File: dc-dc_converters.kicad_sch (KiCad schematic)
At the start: 63 parts, among them J3 JST_SH_1x4_SM04B-SRSS-TB-LF-SN, J4 Molex_Nano-Fit_1x2_105313-220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, U2 SIC477ED-T1-GE3, U3 AP62301Z6-7, U4 AP62301Z6-7

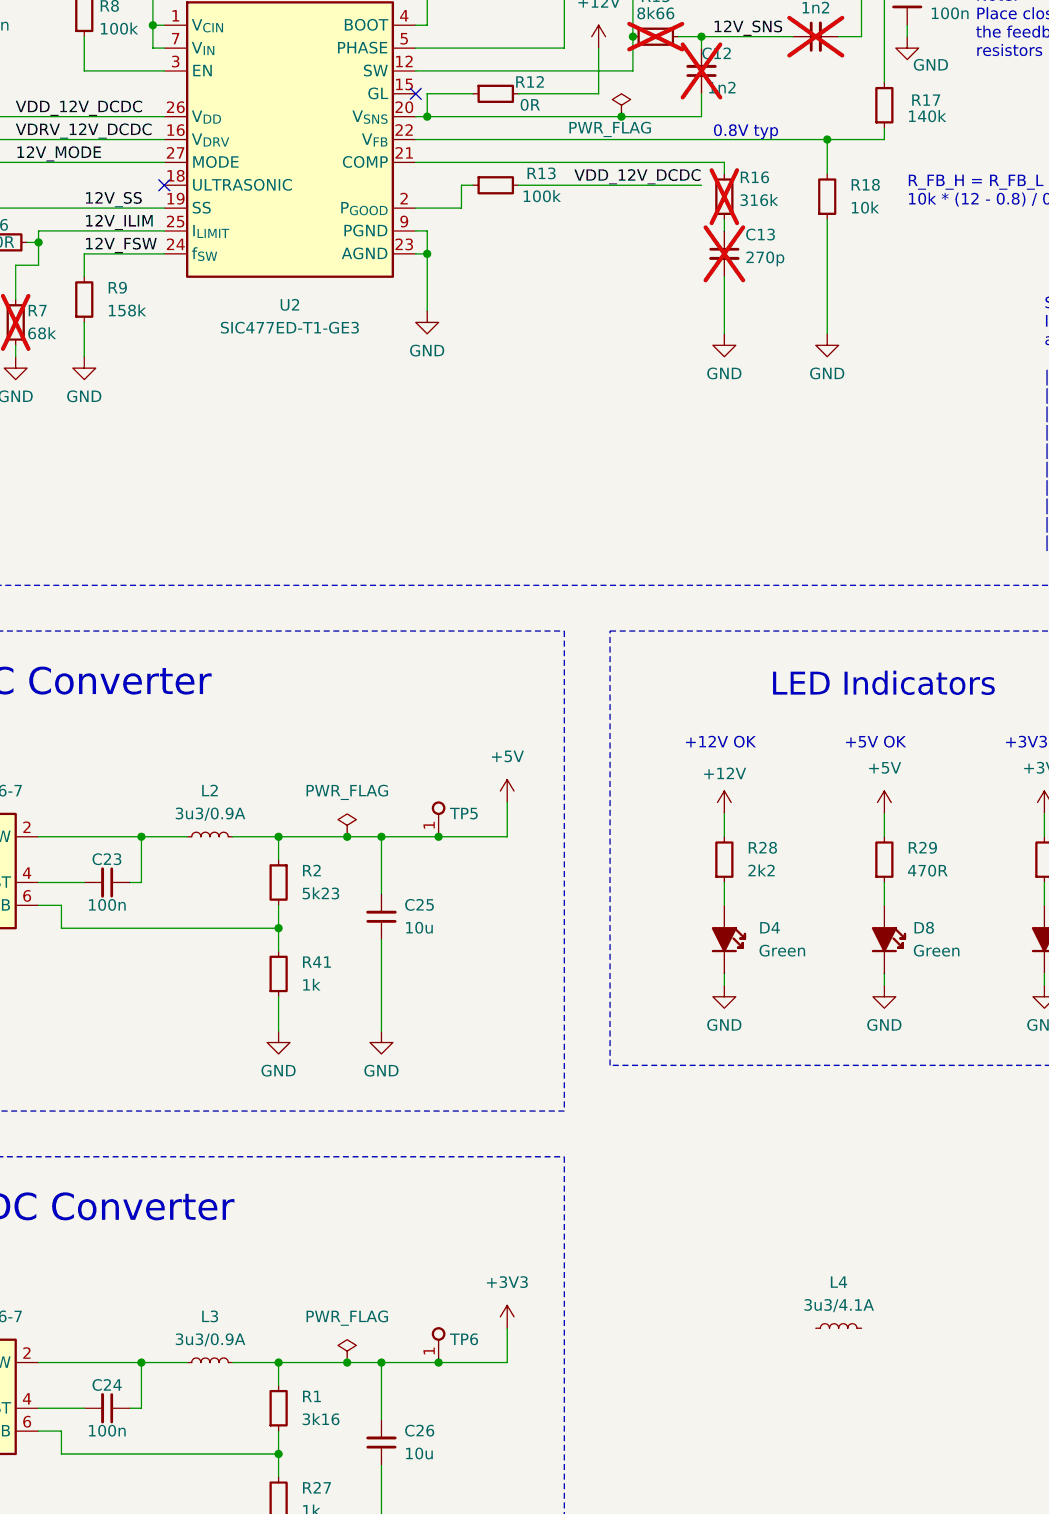
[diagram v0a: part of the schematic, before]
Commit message: [#57006] Change L2 and L3
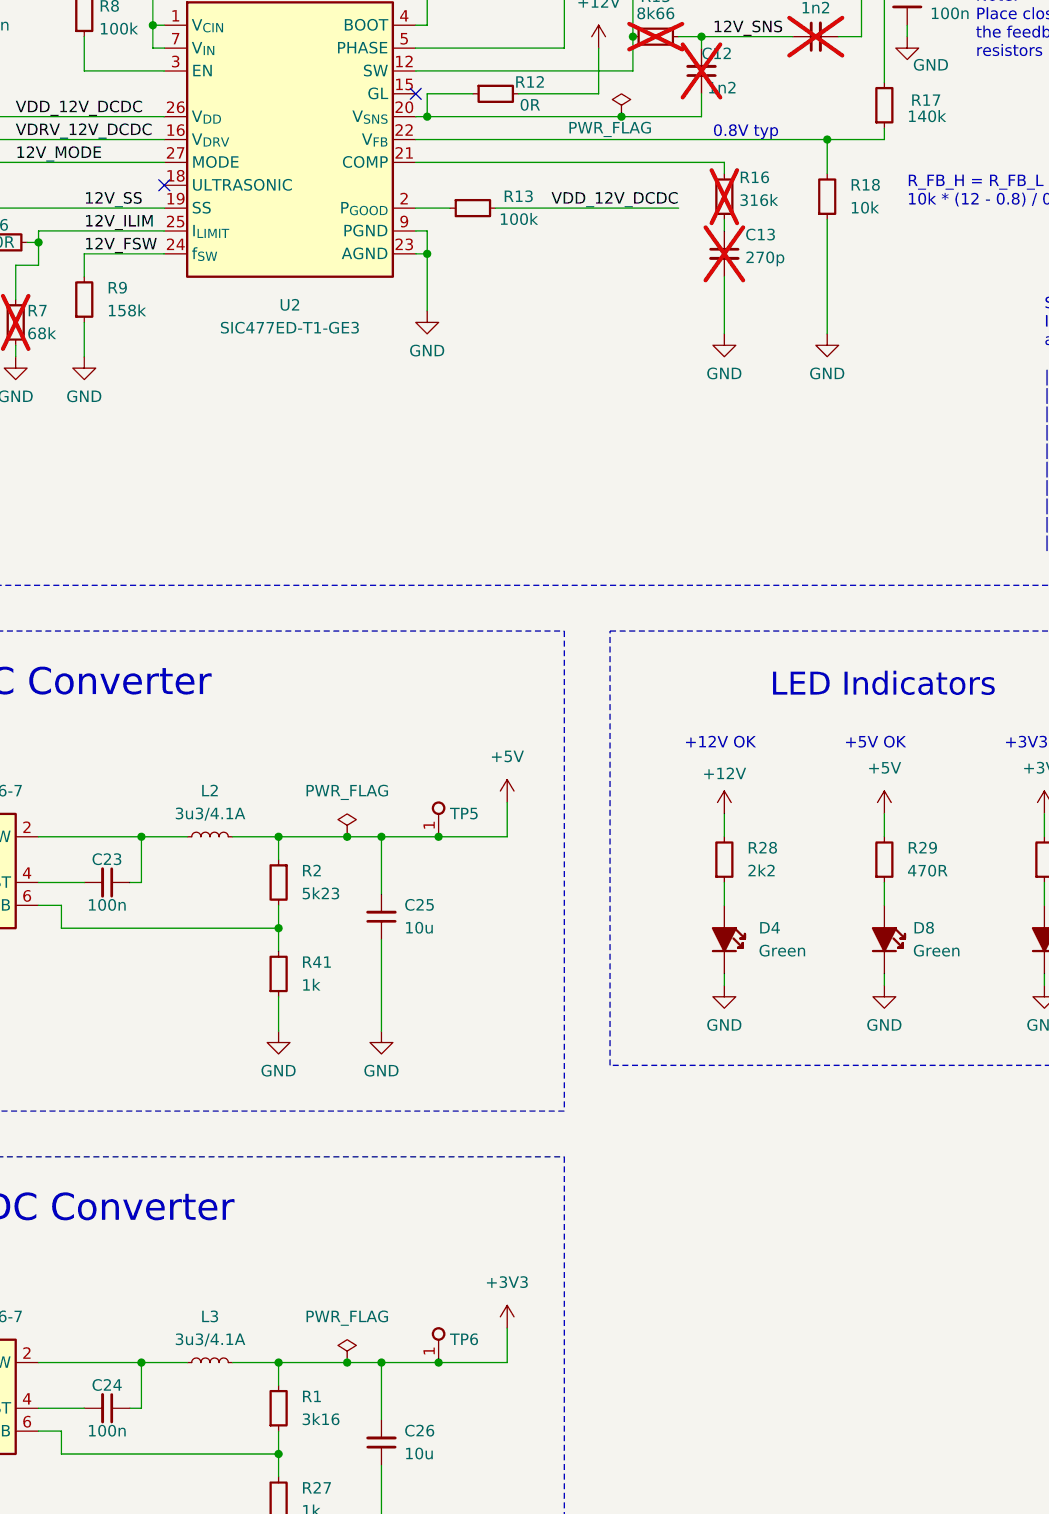
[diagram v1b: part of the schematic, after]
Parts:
- removed L2, L3: L_3u3_0.9A_0805, antmicro-footprints:L_0805_2012Metric, symbol antmicroFixedInductors:L_3u3_0.9A_0805
- removed L4: L_3u3_4.1A_WE-LHMI-5030, antmicro-footprints:L_WE-LHMI-5030, symbol antmicroFixedInductors:L_3u3_4.1A_WE-LHMI-5030
- added L2, L3: L_3u3_4.1A_WE-LHMI-5030, antmicro-footprints:L_WE-LHMI-5030, symbol antmicroFixedInductors:L_3u3_4.1A_WE-LHMI-5030
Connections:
- net +3V3: now also L3.2
- net +5V: now also L2.2
- net at C23.1, U3.2 (SW): now also L2.1
- net at C24.1, U4.2 (SW): now also L3.1
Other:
- moved on the sheet: R13

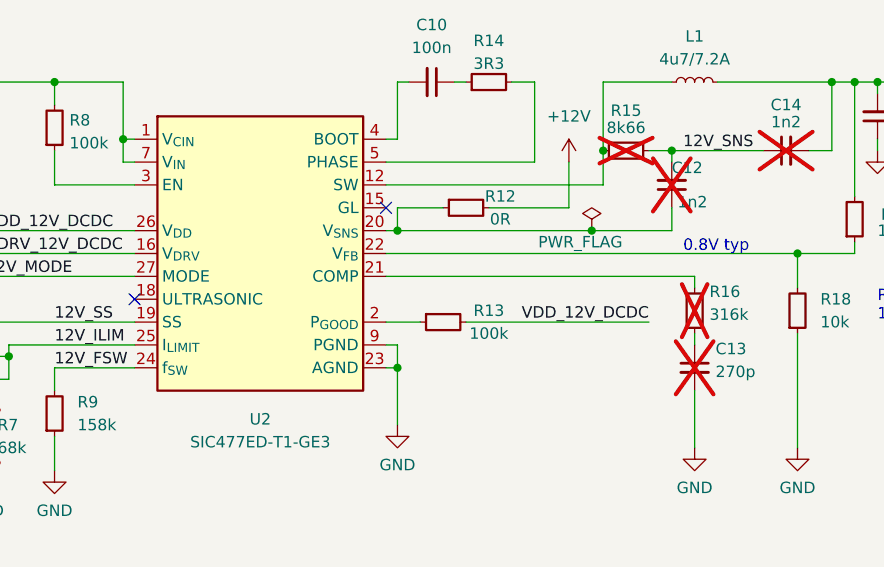
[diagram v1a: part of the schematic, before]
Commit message: [#57006] Update SIC477 from library
Add note about NC pin 21
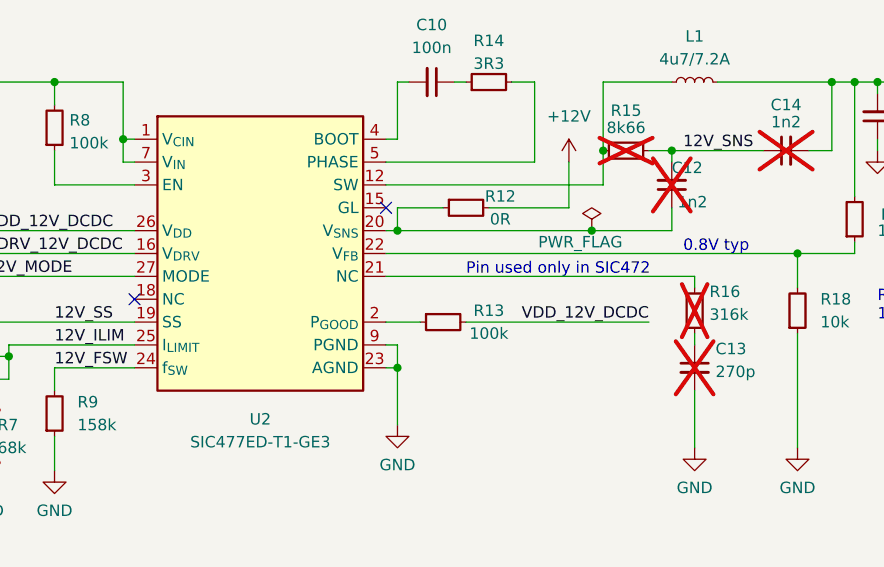
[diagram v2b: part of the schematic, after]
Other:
- note added: "Pin used only in SIC472"
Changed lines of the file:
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@@
   (junction (at 146.05 228.6) (diameter 0) (color 0 0 0 0)
   )
+  (no_connect (at 115.57 97.79))
   (no_connect (at 143.51 87.63))
-  (no_connect (at 115.57 97.79))
   (wire (pts (xy 254 73.66) (xy 256.54 73.66))
     (stroke (width 0) (type default))
@@
     (effects (font (size 3 3)) (justify left bottom))
   )
+  (text "Pin used only in SIC472" (at 152.4 95.25 0)
+    (effects (font (size 1.27 1.27)) (justify left bottom))
+  )
   (text "3V3 DC/DC Converter" (at 78.74 213.36 0)

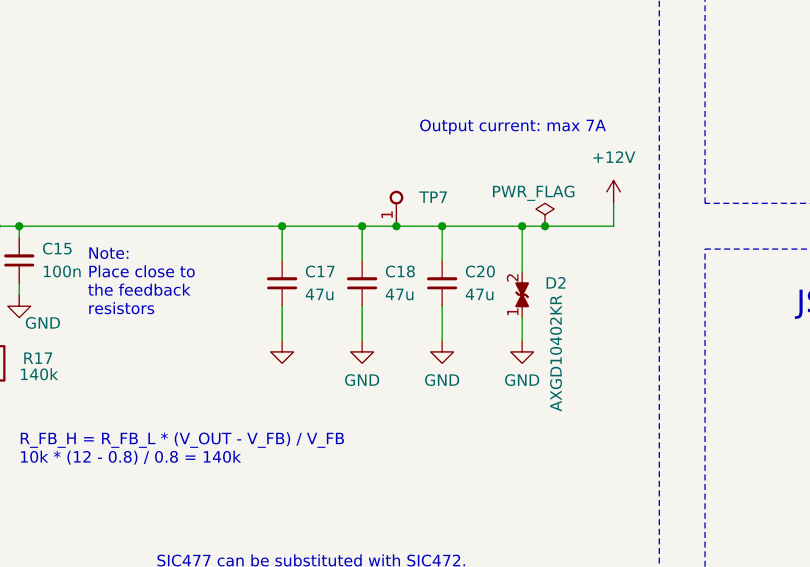
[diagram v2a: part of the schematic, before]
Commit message: [#57006] Change C17, C18, C20 to 25V capacitors
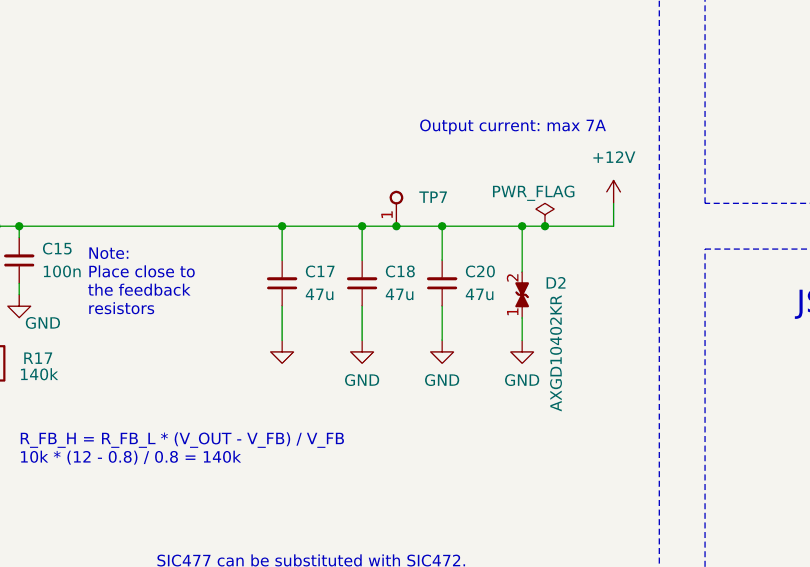
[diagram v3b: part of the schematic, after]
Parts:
- removed C17, C18, C20: C_47u_16V_1206, antmicro-footprints:C_1206_3216Metric, symbol antmicroCapacitorsmisc:C_47u_16V_1206
- added C17, C18, C20: C_47u_25V_1206, antmicro-footprints:C_1206_3216Metric, symbol antmicroCapacitorsmisc:C_47u_25V_1206
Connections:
- net +12V: now also C17.2, C18.2, C20.2
- net GND: now also C17.1, C18.1, C20.1

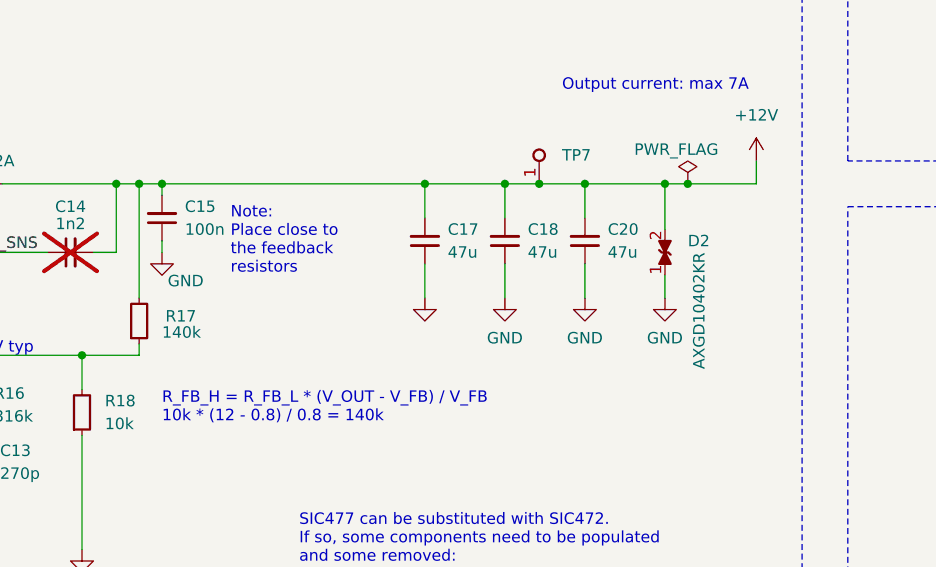
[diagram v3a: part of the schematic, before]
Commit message: [#57006] Add 100u DNP capacitor
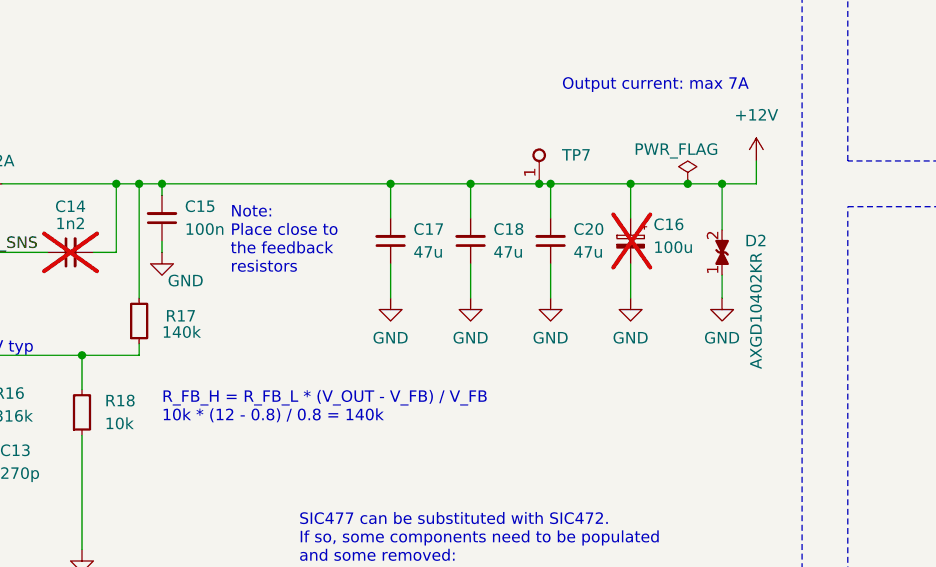
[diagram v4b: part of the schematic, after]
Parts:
- added C16: C_Pol_100u_16V_KEMET-T495-C, antmicro-footprints:C_Pol_EIA-C, symbol antmicroCapacitorspol:C_Pol_100u_16V_KEMET-T495-C
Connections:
- net +12V: now also C16.1
- net GND: now also C16.2
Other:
- moved on the sheet: C17, C18, C20, D2

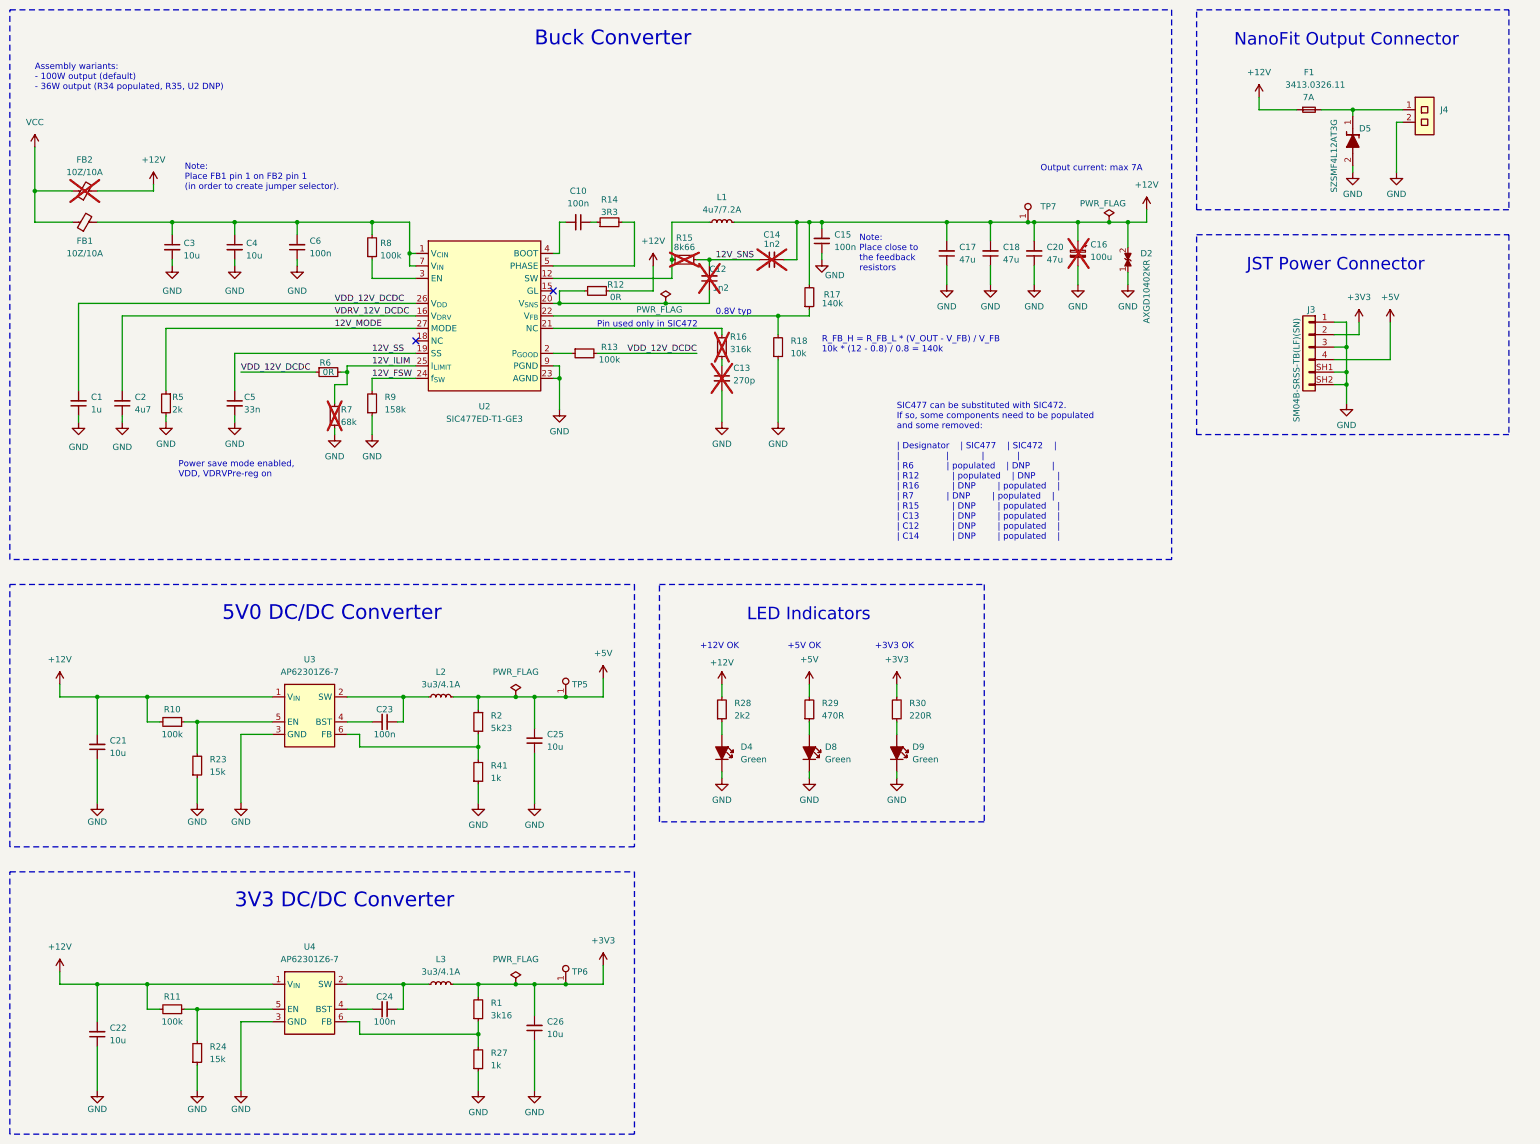
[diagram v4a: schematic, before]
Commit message: [#57225] Finish placement
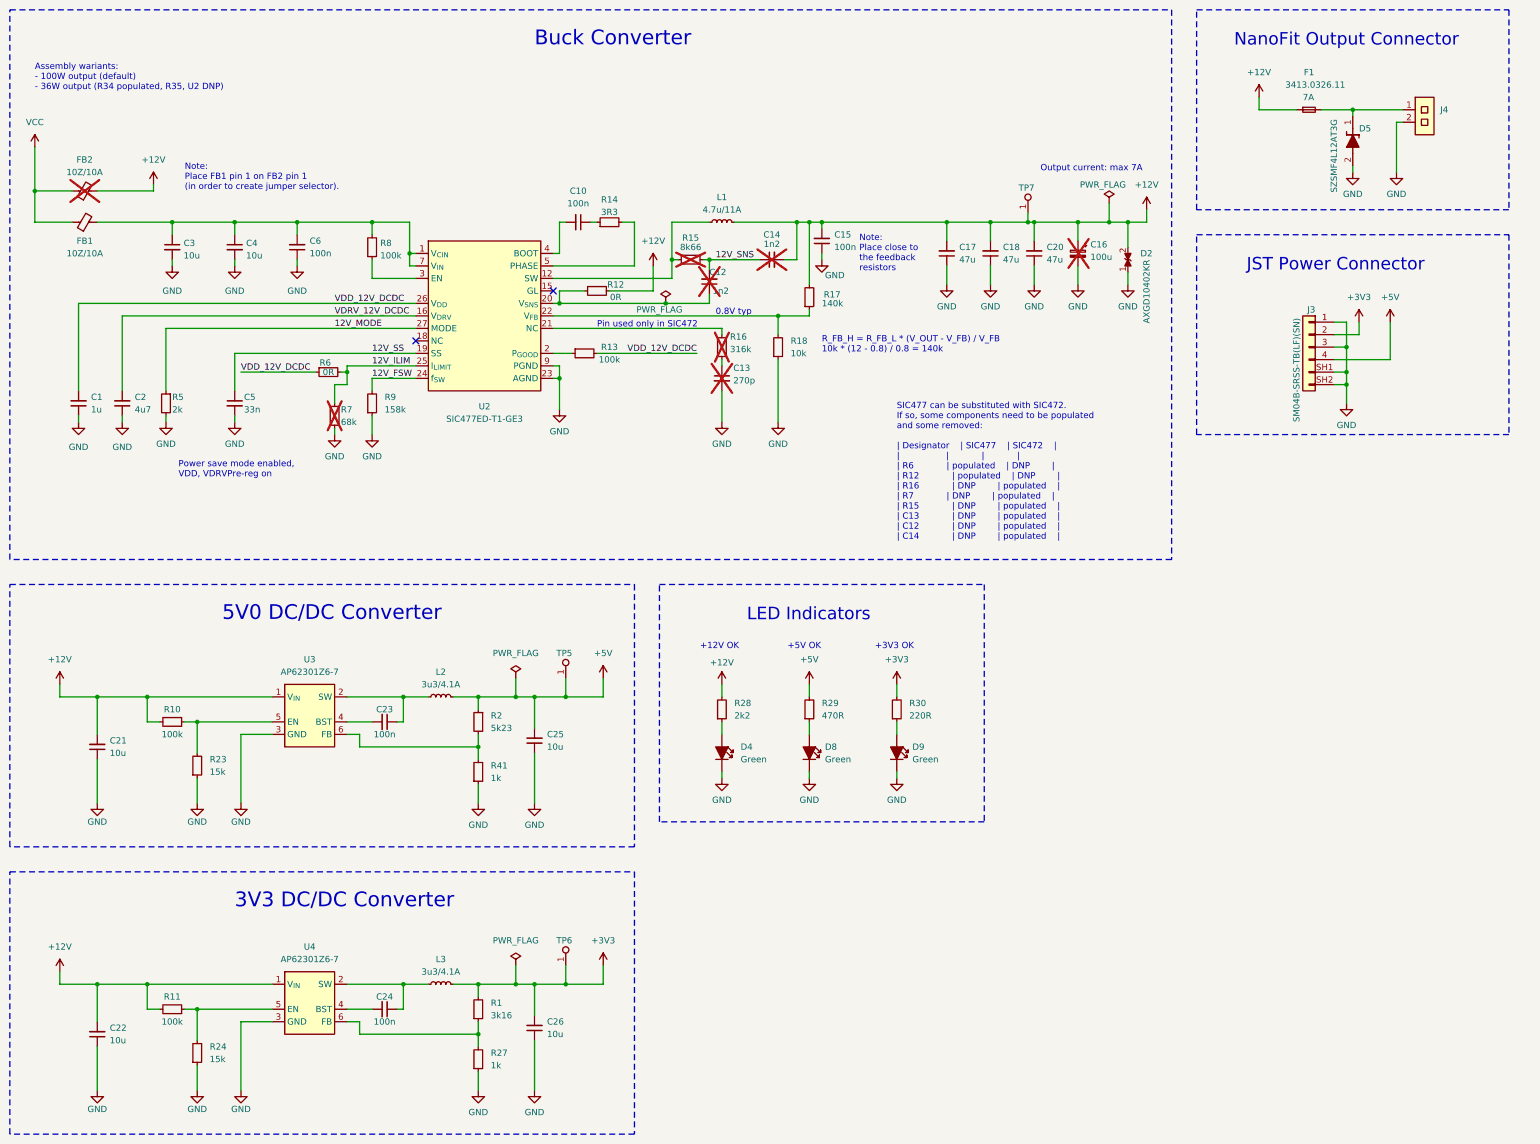
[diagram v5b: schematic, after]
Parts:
- removed L1: L_4u7_7.2A_Vishay-IHLP-3232DZ-5A, antmicro-footprints:L_Vishay-IHLP3232DZ, symbol antmicroFixedInductors:L_4u7_7.2A_Vishay-IHLP-3232DZ-5A
- added L1: L_4u7_11A_Coilcraft-XAL6060, antmicro-footprints:L_Coilcraft-XAL6060, symbol antmicroFixedInductors:L_4u7_11A_Coilcraft-XAL6060
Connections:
- net +12V: now also L1.2
- net at R15.1, U2.12 (SW), U2.13 (SW)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: now also L1.1
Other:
- moved on the sheet: C12, R15, TP5, TP6, TP7
